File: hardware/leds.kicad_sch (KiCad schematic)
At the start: 27 parts, among them U4 SN74LV1T34DBV

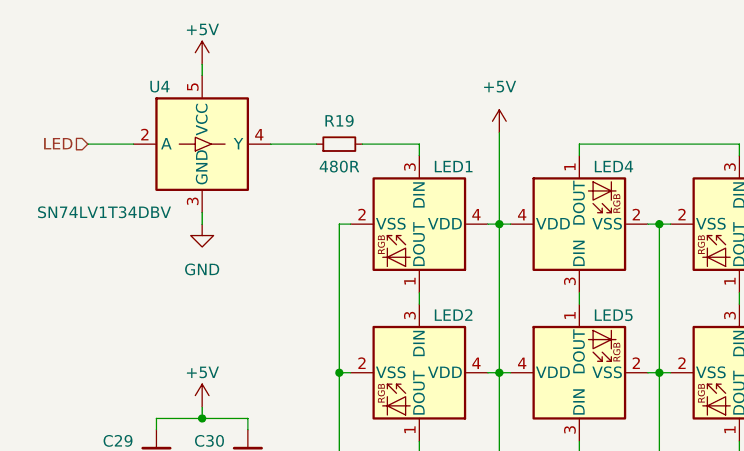
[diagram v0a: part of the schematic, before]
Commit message: Increase DP clearance
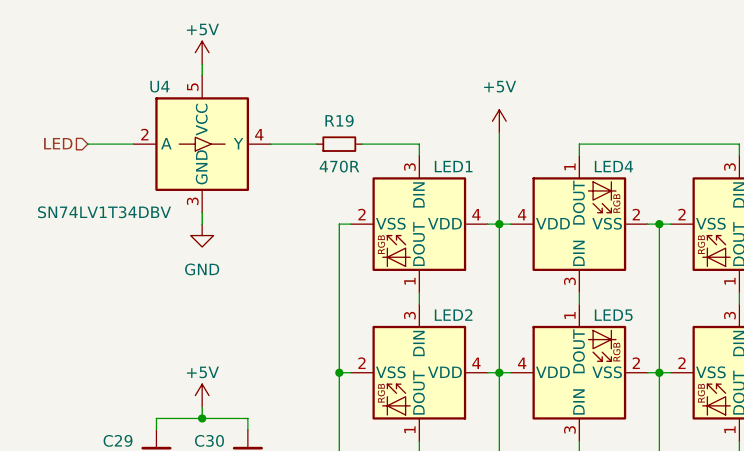
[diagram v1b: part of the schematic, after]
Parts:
- R19: value 480R -> 470R
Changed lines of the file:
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@@
 			)
 		)
-		(property "Value" "480R"
+		(property "Value" "470R"
 			(at 93.98 74.93 90)
 			(effects

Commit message: Add MFR numbers to the passive components
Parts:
- C29: JLCPCB Part # (none) -> C15849
- C30: JLCPCB Part # (none) -> C14663
- R19: JLCPCB Part # (none) -> C23179
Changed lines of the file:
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@@
+			)
+		)
+		(property "JLCPCB Part #" "C23179"
+			(at 93.98 72.39 90)
+			(effects
+				(font
+					(size 1.27 1.27)
+				)
+				(hide yes)
 			)
 		)
@@
 			)
 		)
+		(property "JLCPCB Part #" "C15849"
+			(at 73.66 106.68 0)
+			(effects
+				(font
+					(size 1.27 1.27)
+				)
+				(hide yes)
+			)
+		)
 		(pin "1"
 		)
@@
 			)
 		)
+		(property "JLCPCB Part #" "C14663"
+			(at 83.82 106.68 0)
+			(effects
+				(font
+					(size 1.27 1.27)
+				)
+				(hide yes)
+			)
+		)

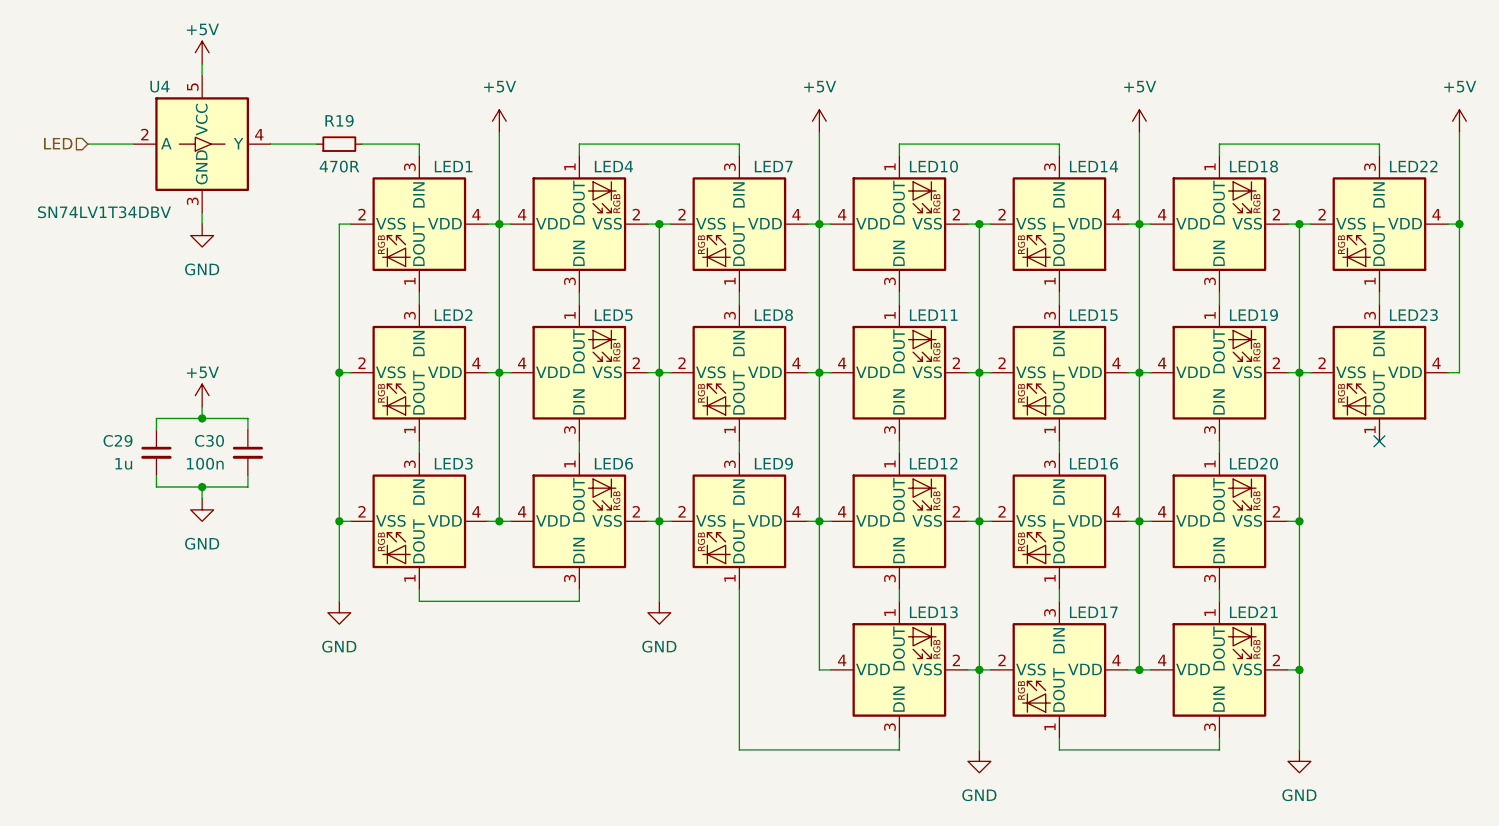
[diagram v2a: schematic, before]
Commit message: Add test points to LED DIN and DOUT
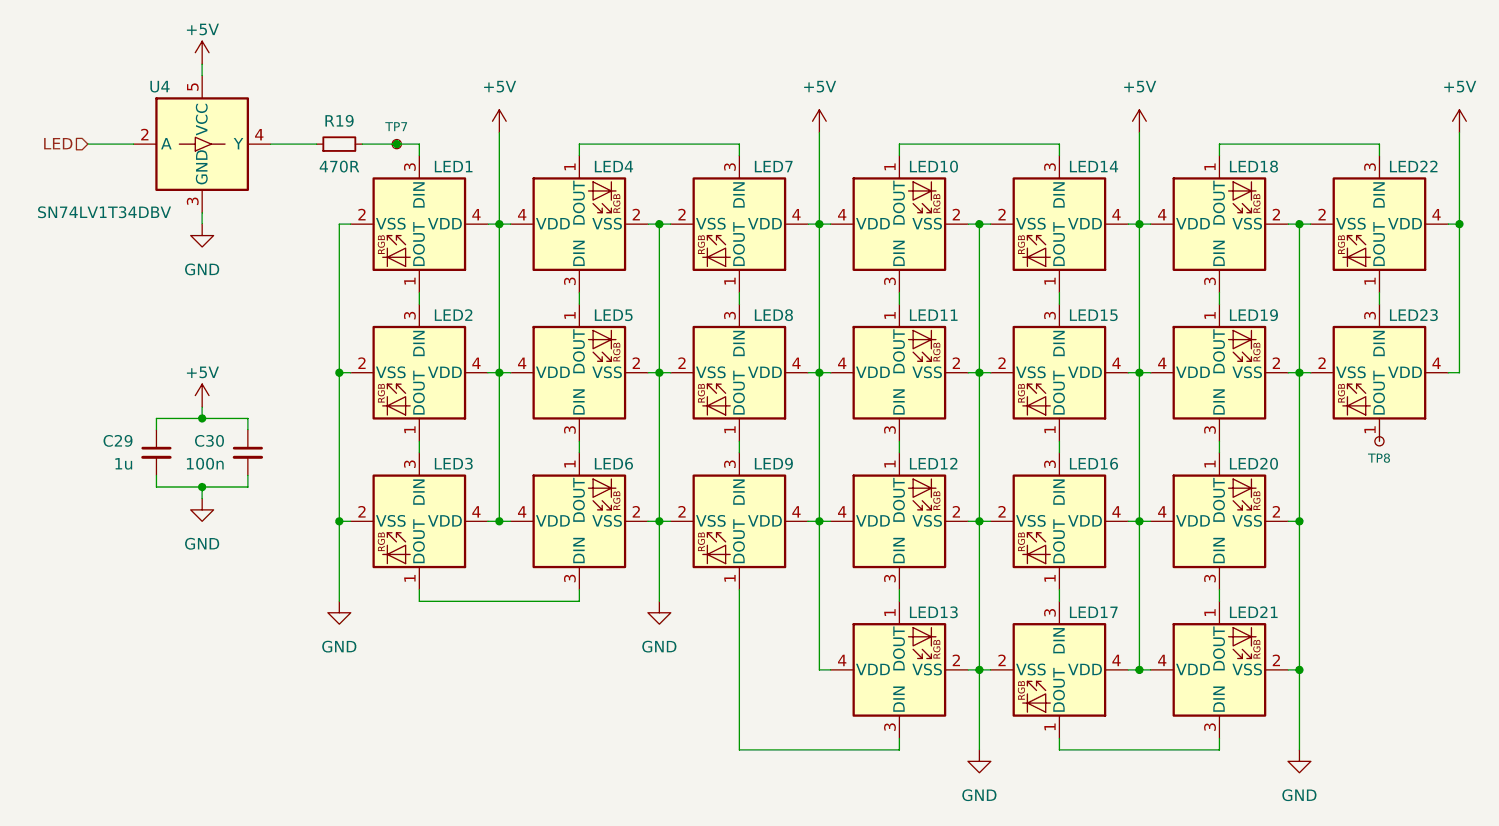
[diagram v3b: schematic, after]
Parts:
- added TP7, TP8: TX, TestPoint:TestPoint_Pad_D1.0mm, symbol Connector:TestPoint_Small
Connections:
- net at LED23.1 (DOUT): now also TP8.1
- net at LED1.3 (DIN), R19.2: now also TP7.1
- no-connect marks 1 -> 0
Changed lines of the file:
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@@
 	)
 	(junction
+		(at 100.3633 72.39)
+		(diameter 0)
+		(color 0 0 0 0)
+	)
+	(junction
 		(at 200.66 97.79)
 		(diameter 0)
@@
 		(color 0 0 0 0)
 	)
-	(no_connect
-		(at 209.55 105.41)
-	)
 	(wire
 		(pts
@@
 	(wire
 		(pts
+			(xy 96.52 72.39) (xy 100.3633 72.39)
+		)
+		(stroke
+			(width 0)
+			(type default)
+		)
+	)
+	(wire
+		(pts
 			(xy 156.21 72.39) (xy 156.21 73.66)
 		)
@@
 	(wire
 		(pts
-			(xy 102.87 72.39) (xy 96.52 72.39)
+			(xy 102.87 72.39) (xy 100.3633 72.39)
 		)
 		(stroke
@@
 	)
 	(symbol
+		(lib_id "Connector:TestPoint_Small")
+		(at 100.3633 72.39 0)
+		(unit 1)
+		(exclude_from_sim no)
+		(in_bom no)
+		(on_board yes)
+		(dnp no)
+		(property "Reference" "TP7"
+			(at 100.3633 70.485 0)
+			(effects
+				(font
+					(size 1 1)
+				)
+			)
+		)
+		(property "Value" "TX"
+			(at 101.6333 74.295 0)
+			(effects
+				(font
+					(size 1.27 1.27)
+				)
+				(justify left)
+				(hide yes)
+			)
+		)
+		(property "Footprint" "TestPoint:TestPoint_Pad_D1.0mm"
+			(at 105.4433 72.39 0)
+			(effects
+				(font
+					(size 1.27 1.27)
+				)
+				(hide yes)
+			)
+		)
+		(property "Datasheet" "~"
+			(at 105.4433 72.39 0)
+			(effects
+				(font
+					(size 1.27 1.27)
+				)
+				(hide yes)
+			)
+		)
+		(property "Description" ""
+			(at 100.3633 72.39 0)
+			(effects
+				(font
+					(size 1.27 1.27)
+				)
+			)
+		)
+		(pin "1"
+		)
+		(instances
+			(project "katia"
+				(path "/4cc5d416-57f5-4147-8183-e03ae6b1198a/089db7cd-2934-428b-a62a-55e0735649ba/364701ca-c0a6-43f9-8444-ed2021756e6c"
+					(reference "TP7")
+					(unit 1)
+				)
+				(path "/4cc5d416-57f5-4147-8183-e03ae6b1198a/50d96a5e-3d25-4129-9495-15388c76587f/71fa2931-3753-408f-9328-62d662f82c2b"
+					(reference "TP12")
+					(unit 1)
+				)
+			)
+		)
+	)
+	(symbol
 		(lib_id "LED:SK6812MINI")
 		(at 120.65 81.28 90)
@@
 					(unit 1)
 				)
+			)
+		)
+	)
+	(symbol
+		(lib_id "Connector:TestPoint_Small")
+		(at 209.55 105.41 0)
+		(unit 1)
+		(exclude_from_sim no)
+		(in_bom no)
+		(on_board yes)
+		(dnp no)
+		(property "Reference" "TP8"
+			(at 209.55 107.315 0)
+			(effects
+				(font
+					(size 1 1)
+				)
+			)
+		)
+		(property "Value" "TX"
+			(at 210.82 107.315 0)
+			(effects
+				(font
+					(size 1.27 1.27)
+				)
+				(justify left)
+				(hide yes)
+			)
+		)
+		(property "Footprint" "TestPoint:TestPoint_Pad_D1.0mm"
+			(at 214.63 105.41 0)
+			(effects
+				(font
+					(size 1.27 1.27)
+				)
+				(hide yes)
+			)
+		)
+		(property "Datasheet" "~"
+			(at 214.63 105.41 0)
+			(effects
+				(font
+					(size 1.27 1.27)
+				)
+				(hide yes)
+			)
+		)
+		(property "Description" ""
+			(at 209.55 105.41 0)
+			(effects
+				(font
+					(size 1.27 1.27)
+				)
+			)
+		)
+		(pin "1"
+		)
+		(instances
+			(project "katia"
+				(path "/4cc5d416-57f5-4147-8183-e03ae6b1198a/089db7cd-2934-428b-a62a-55e0735649ba/364701ca-c0a6-43f9-8444-ed2021756e6c"
+					(reference "TP8")
+					(unit 1)
+				)
+				(path "/4cc5d416-57f5-4147-8183-e03ae6b1198a/50d96a5e-3d25-4129-9495-15388c76587f/71fa2931-3753-408f-9328-62d662f82c2b"
+					(reference "TP13")
+					(unit 1)
+				)
